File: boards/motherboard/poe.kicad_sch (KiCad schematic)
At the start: 50 parts, among them Q1 FDC2512, T1 HR051067, U2 TPS23753APWR, U3 FOD817AS, U4 TLV341ASN1

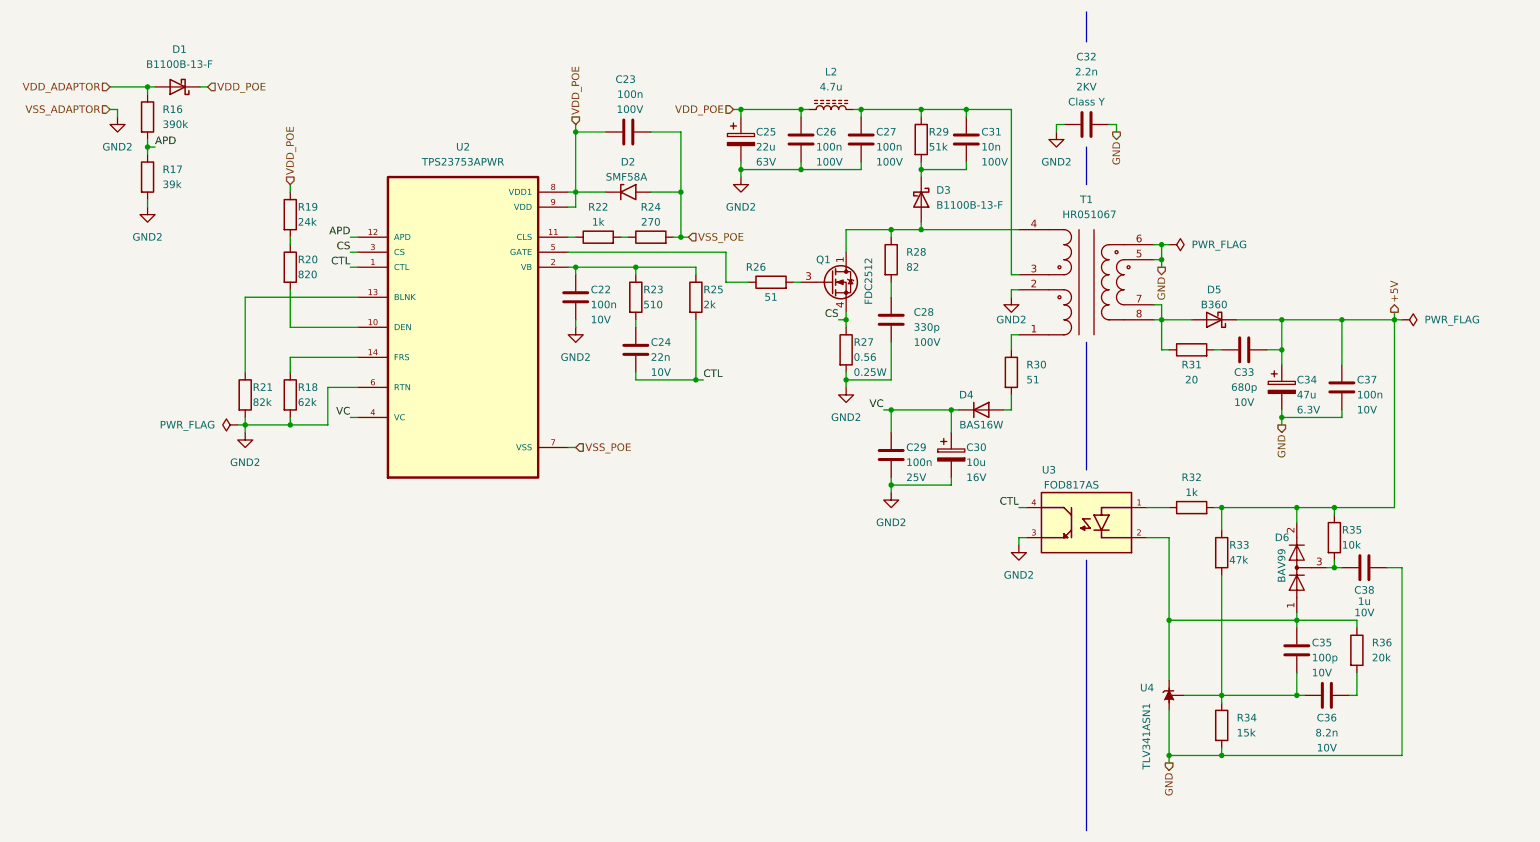
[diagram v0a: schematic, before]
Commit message: feat: assign footprints
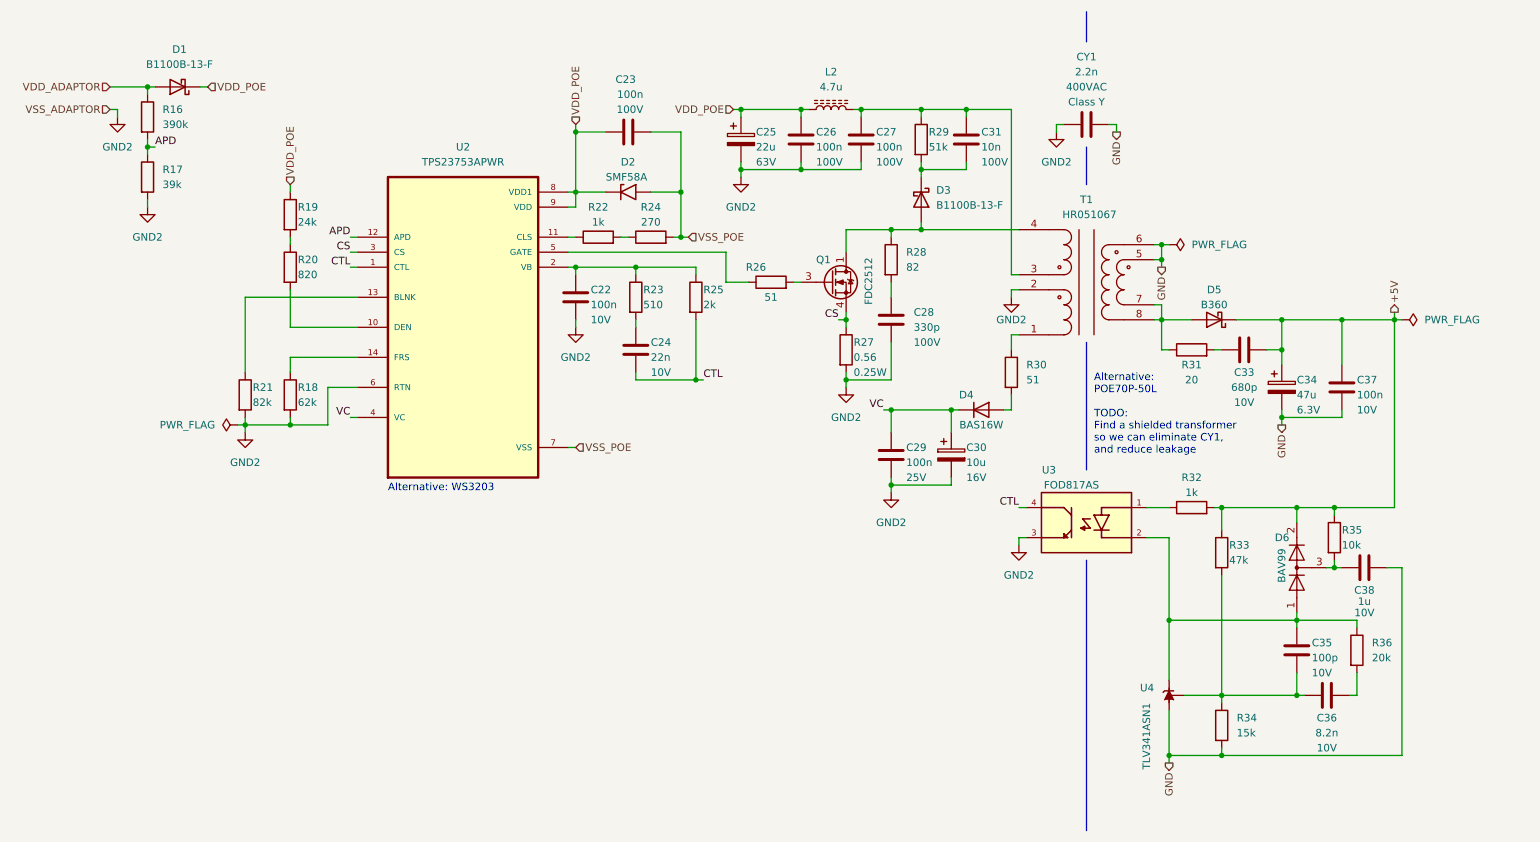
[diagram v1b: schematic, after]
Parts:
- C22, C23, C24, C26, C27, C28, C29, C31, C33, C35, C36, C37, C38: footprint (none) -> Capacitor_SMD:C_0603_1608Metric
- C25, C30, C34: footprint (none) -> Capacitor_SMD:CP_Elec_4x5.4
- CY1: renamed from C32; footprint (none) -> Capacitor_THT:C_Disc_D10.5mm_W5.0mm_P10.00mm; Voltage Rating 2KV -> 400VAC
- D1, D3: footprint (none) -> Diode_SMD:D_SMB
- L2: footprint (none) -> Inductor_SMD:L_0805_2012Metric
- R16, R17, R18, R19, R20, R21, R22, R23, R24, R25, R26, R28, R29, R30, R31, R32, R33, R34, R35, R36: footprint (none) -> Resistor_SMD:R_0603_1608Metric
- R27: footprint (none) -> Resistor_SMD:R_1206_3216Metric
- T1: footprint (none) -> footprints:XFMR-SMD_HR051067
- U2: footprint TPS23753APWR:SOP65P640X120-14N -> Package_SO:TSSOP-14_4.4x5mm_P0.65mm
- U3: footprint FOD817AS:SOIC254P1016X385-4N -> footprints:SOIC254P1016X385-4N
- U4: footprint (none) -> Package_TO_SOT_SMD:SOT-23-3
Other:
- note added: "Alternative: POE70P-50L TODO: Find a shielded transformer so we can eliminate CY1, and reduce leakage"
- note added: "Alternative: WS3203"

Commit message: feat: first release of motherboard
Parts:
- removed C30: 10u, Capacitor_SMD:CP_Elec_4x5.4, symbol Device:C_Polarized
- removed C34: 47u, Capacitor_SMD:CP_Elec_4x5.4, symbol Device:C_Polarized
- removed D1, D3: B1100B-13-F, Diode_SMD:D_SMB, symbol B1100B-13-F:B1100B-13-F
- removed Q1: FDC2512, Package_TO_SOT_SMD:SuperSOT-6, symbol Transistor_FET:FDC2512
- removed R16: 390k, Resistor_SMD:R_0603_1608Metric, symbol Device:R
- removed R17: 39k, Resistor_SMD:R_0603_1608Metric, symbol Device:R
- removed R19: 24k, Resistor_SMD:R_0603_1608Metric, symbol Device:R
- removed R24: 270, Resistor_SMD:R_0603_1608Metric, symbol Device:R
- added C17: 10u, Capacitor_SMD:C_0603_1608Metric, symbol Device:C
- added C34, C47: 47u, Capacitor_SMD:C_0603_1608Metric, symbol Device:C
- added D3: S1B-13-F, Diode_SMD:D_SMA, symbol Device:D
- added Q1: FDC86244, Package_TO_SOT_SMD:SuperSOT-6, symbol Transistor_FET:FDC86244
- C22, C29, C37: LCSC PN (none) -> C14663
- C23, C26, C27: LCSC PN (none) -> C15725
- C24: LCSC PN (none) -> C21122
- C25: footprint Capacitor_SMD:CP_Elec_4x5.4 -> Capacitor_SMD:CP_Elec_6.3x7.7; LCSC PN (none) -> C267472
- C28: LCSC PN (none) -> C126579
- C31: LCSC PN (none) -> C107059
- C33: LCSC PN (none) -> C1630
- C35: LCSC PN (none) -> C14858
- C36: LCSC PN (none) -> C1322360
- C38: LCSC PN (none) -> C15849
- CY1: LCSC PN (none) -> C499511
- D2: value SMF58A -> SMAJ58A; footprint Diode_SMD:D_SMF -> Diode_SMD:D_SMA; LCSC PN (none) -> C110521
- D4: LCSC PN (none) -> C56624
- D5: value B360 -> SS34; footprint Diode_SMD:D_SMC -> Diode_SMD:D_SMA; LCSC PN (none) -> C8678
- D6: LCSC PN (none) -> C2500
- L2: footprint Inductor_SMD:L_0805_2012Metric -> Inductor_SMD:L_1008_2520Metric; LCSC PN (none) -> C82314
- R18: LCSC PN (none) -> C23254
- R20: value 820 -> 24.9k; LCSC PN (none) -> C2930080
- R21: LCSC PN (none) -> C23221
- R22: value 1k -> 1.27k; LCSC PN (none) -> C2930048
- R23: LCSC PN (none) -> C23193
- R25: value 2k -> 2.2k; LCSC PN (none) -> C4190
- R26, R30: LCSC PN (none) -> C23197
- R27: LCSC PN (none) -> C2907358
- R28: LCSC PN (none) -> C23255
- R29: LCSC PN (none) -> C23196
- R31: LCSC PN (none) -> C22950
- R32: LCSC PN (none) -> C21190
- R33: LCSC PN (none) -> C25819
- R34: LCSC PN (none) -> C22809
- R35: LCSC PN (none) -> C25804
- R36: LCSC PN (none) -> C4184
- T1: Datasheet_1 https://lcsc.com/product-detail/Power-Transformer_Zhongshan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 -> (none); Footprint_1 HR051067:XFMR-SMD_HR051067 -> (none); Reference_1 T -> (none); Value_1 HR051067 -> (none)
- U2: Availability In Stock -> (none); Check_prices https://www.snapeda.com/parts/TPS23753APWR/Texas+Instrument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 -> (none); LCSC PN (none) -> C92115; MF Texas Instruments -> (none); MP TPS23753APWR -> (none); Package TSSOP-14 Texas Instruments -> (none); Price None -> (none); SnapEDA_Link https://www.snapeda.com/parts/TPS23753APWR/Texas+Instrument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 -> (none)
- U3: value FOD817AS -> FOD817ASD; Availability In Stock -> (none); LCSC PN (none) -> C241830; MANUFACTURER FAIRCHILD SEMICONDUCTOR -> (none); MF ON -> (none); MP FOD817AS -> (none); Package SMD-4 ON Semiconductor -> (none)
- U4: value TLV341ASN1 -> TLV431ASN1; LCSC PN (none) -> C127592
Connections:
- net APD is gone; now on net GND2: U2.12 (APD)
- net +5V: now also C34.1, C47.1
- net CS: now also Q1.4 (S)
- net GND: now also C34.2, C47.2
- net GND2: now also C17.2
- net VC: now also C17.1
- net VDD_POE: now also R20.1
- net VSS_POE: now also R22.2
- net at C31.2, R29.2: now also D3.1 (K)
- net at R28.1, T1.4: now also D3.2 (A), Q1.1 (D), Q1.2 (D), Q1.5 (D), Q1.6 (D)
- net at R26.2: now also Q1.3 (G)
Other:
- moved on the sheet: C37, R20, R22

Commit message: feat: revised motherboard
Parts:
- C23, C26, C27: footprint Capacitor_SMD:C_0603_1608Metric -> Capacitor_SMD:C_0805_2012Metric; LCSC PN C15725 -> C28233
- C34, C47: footprint Capacitor_SMD:C_0603_1608Metric -> Capacitor_SMD:C_1206_3216Metric
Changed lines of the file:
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@@
 			)
 		)
-		(property "Footprint" "Capacitor_SMD:C_0603_1608Metric"
+		(property "Footprint" "Capacitor_SMD:C_1206_3216Metric"
 			(at 233.3752 81.28 0)
 			(effects
@@
 			)
 		)
-		(property "Footprint" "Capacitor_SMD:C_0603_1608Metric"
+		(property "Footprint" "Capacitor_SMD:C_0805_2012Metric"
 			(at 162.2552 39.37 0)
 			(effects
@@
 			)
 		)
-		(property "LCSC PN" "C15725"
+		(property "LCSC PN" "C28233"
 			(at 161.29 35.56 0)
 			(effects
@@
 			)
 		)
-		(property "Footprint" "Capacitor_SMD:C_0603_1608Metric"
+		(property "Footprint" "Capacitor_SMD:C_1206_3216Metric"
 			(at 242.2652 81.28 0)
 			(effects
@@
 			)
 		)
-		(property "Footprint" "Capacitor_SMD:C_0603_1608Metric"
+		(property "Footprint" "Capacitor_SMD:C_0805_2012Metric"
 			(at 152.0952 39.37 0)
 			(effects
@@
 			)
 		)
-		(property "LCSC PN" "C15725"
+		(property "LCSC PN" "C28233"
 			(at 151.13 35.56 0)
 			(effects
@@
 			)
 		)
-		(property "Footprint" "Capacitor_SMD:C_0603_1608Metric"
+		(property "Footprint" "Capacitor_SMD:C_0805_2012Metric"
 			(at 125.73 33.3248 0)
 			(effects
@@
 			)
 		)
-		(property "LCSC PN" "C15725"
+		(property "LCSC PN" "C28233"
 			(at 121.92 34.29 90)
 			(effects
